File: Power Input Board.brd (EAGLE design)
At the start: 136.7 x 135.2 mm, 10 parts, among them Q1 SPB80P06P

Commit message: put in outline
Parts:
- moved Q1 114.9 mm to (92.7, 36.8)
- moved D4 112.0 mm to (80.0, 27.9)
- moved U$1 107.3 mm to (72.4, 38.1)
- moved R3 92.7 mm to (69.8, 26.7)
- moved D2 83.3 mm to (62.2, 33.0)
- moved D3 82.9 mm to (55.9, 38.1)
- moved D1 79.5 mm to (62.2, 39.4)
- moved R2 76.3 mm to (57.1, 31.8)
- moved R1 76.2 mm to (61.0, 27.9)
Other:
- board size 136.7 x 135.2 mm -> 136.7 x 125.3 mm

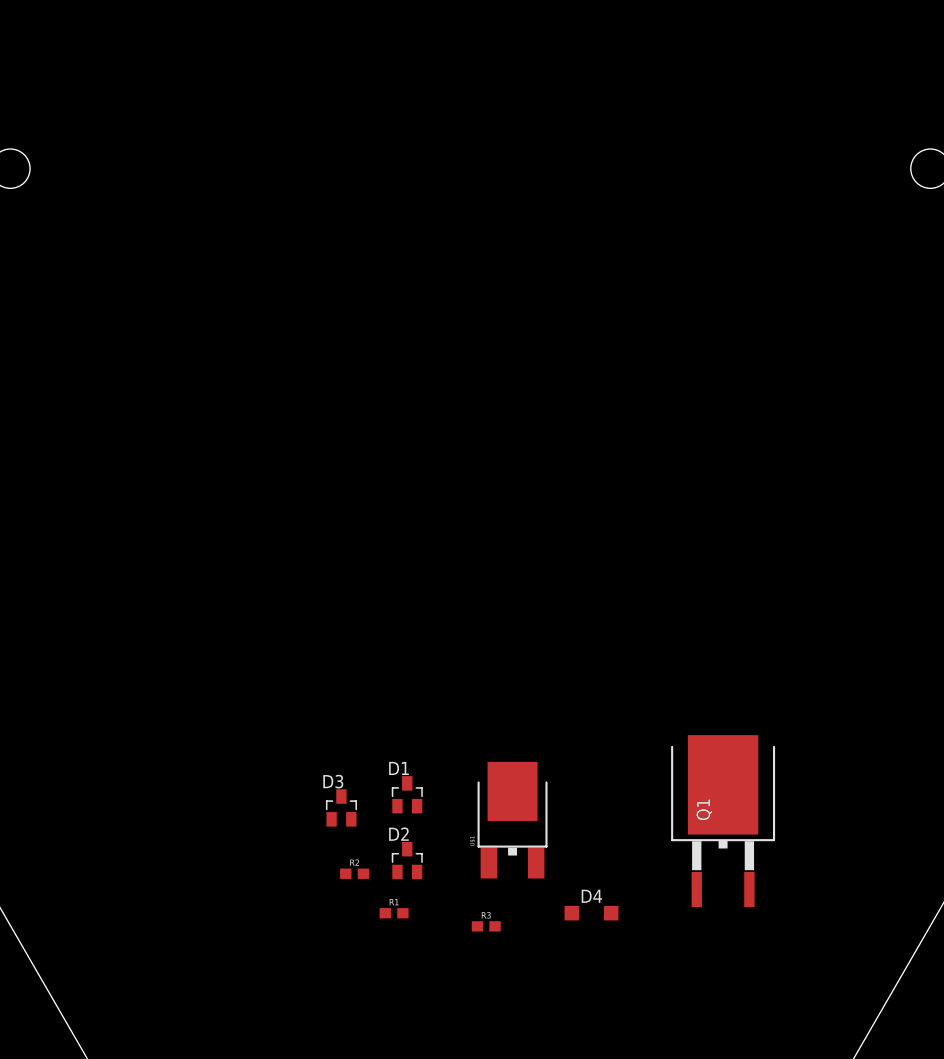
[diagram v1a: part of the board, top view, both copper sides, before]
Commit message: added brick outlines
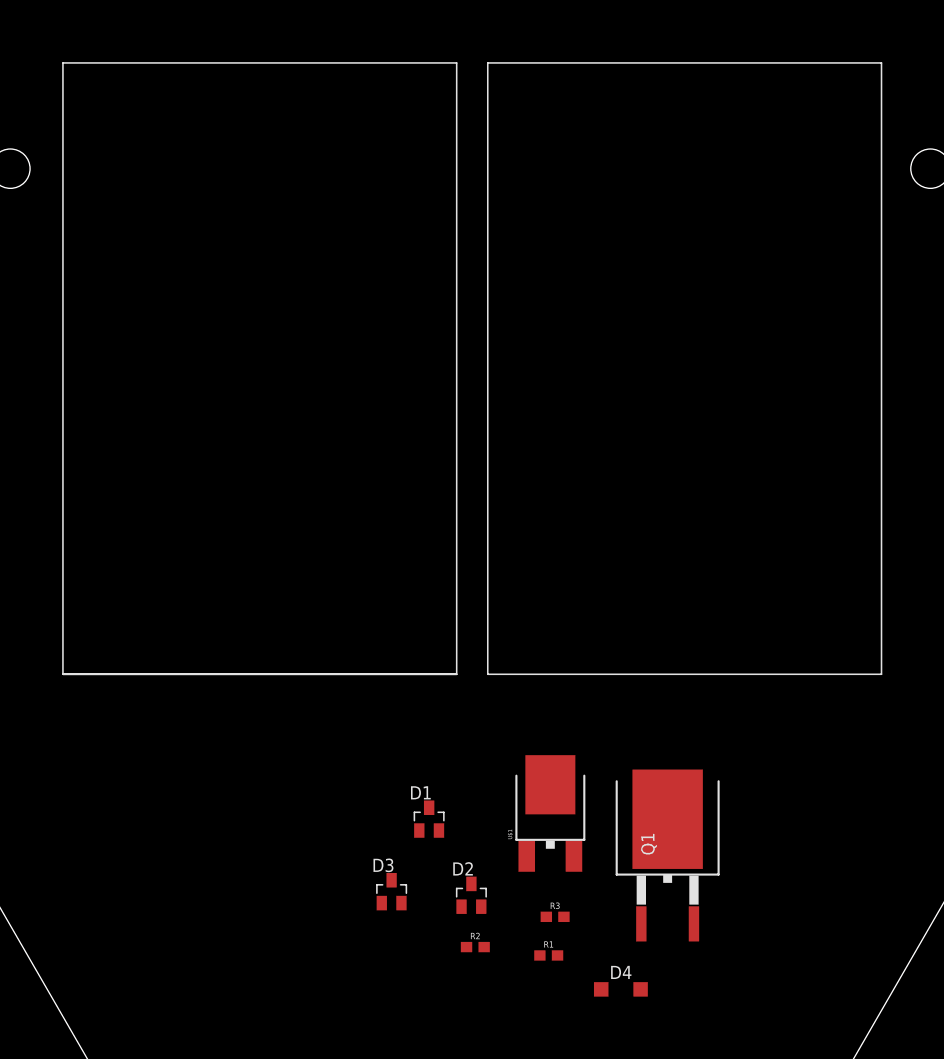
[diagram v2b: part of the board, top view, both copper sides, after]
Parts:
- moved R1 15.5 mm to (75.9, 23.9)
- moved R2 13.6 mm to (68.8, 24.7)
- moved D3 9.42 mm to (60.7, 30.0)
- moved D4 7.88 mm to (82.8, 20.6)
- moved D2 7.04 mm to (68.4, 29.7)
- moved R3 6.71 mm to (76.5, 27.6)
- moved Q1 6.30 mm to (87.4, 33.5)
- moved U$1 3.71 mm to (76.0, 38.8)
- moved D1 3.16 mm to (64.3, 37.0)

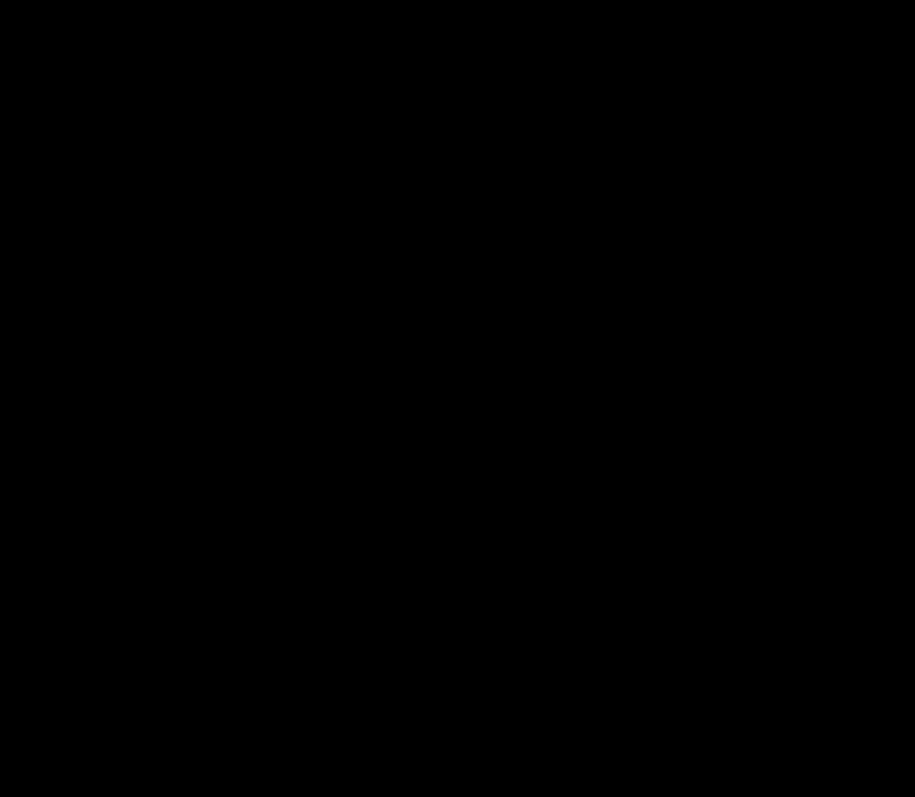
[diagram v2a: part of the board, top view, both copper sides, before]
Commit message: inserted diodes
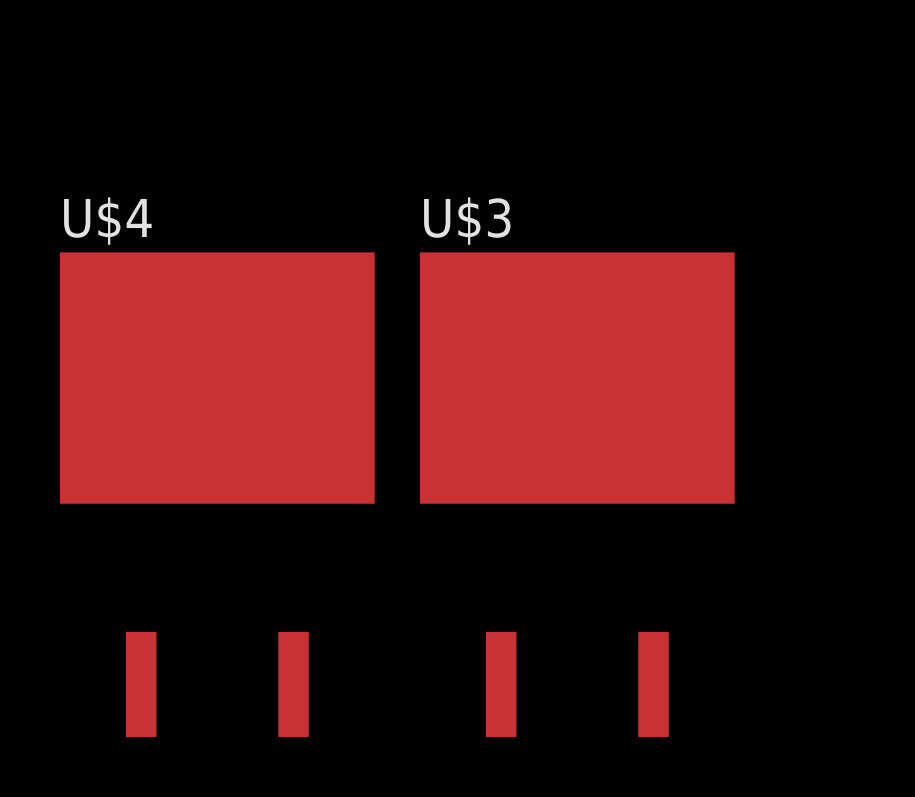
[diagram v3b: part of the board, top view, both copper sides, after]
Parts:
- added U$3, U$4: DIODE, DIODE:DIODE
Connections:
- new net +12V: U$3.OUT, U$4.OUT
- new net +12V_1: U$3.IN1, U$3.IN2
- new net +12V_2: U$4.IN1, U$4.IN2
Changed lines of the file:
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@@
 </element>
 <element name="U$2" library="board_outlines" package="PDB" value="BOARDPDB" x="0" y="0"/>
+<element name="U$3" library="DIODE" package="DIODE" value="DIODE" x="-12" y="7"/>
+<element name="U$4" library="DIODE" package="DIODE" value="DIODE" x="-24" y="7"/>
 </elements>
 <signals>
@@
 <contactref element="Q1" pad="1"/>
 </signal>
+<signal name="+12V_1">
+<contactref element="U$3" pad="IN1"/>
+<contactref element="U$3" pad="IN2"/>
+<wire x1="-4.215" y1="0.977" x2="-9.295" y2="0.977" width="0" layer="19" extent="1-1"/>
+</signal>
+<signal name="+12V_2">
+<contactref element="U$4" pad="IN1"/>
+<contactref element="U$4" pad="IN2"/>
+<wire x1="-16.215" y1="0.977" x2="-21.295" y2="0.977" width="0" layer="19" extent="1-1"/>
+</signal>
+<signal name="+12V">
+<contactref element="U$3" pad="OUT"/>
+<contactref element="U$4" pad="OUT"/>
+<wire x1="-6.755" y1="11.19" x2="-18.755" y2="11.19" width="0" layer="19" extent="1-1"/>
+</signal>
 </signals>

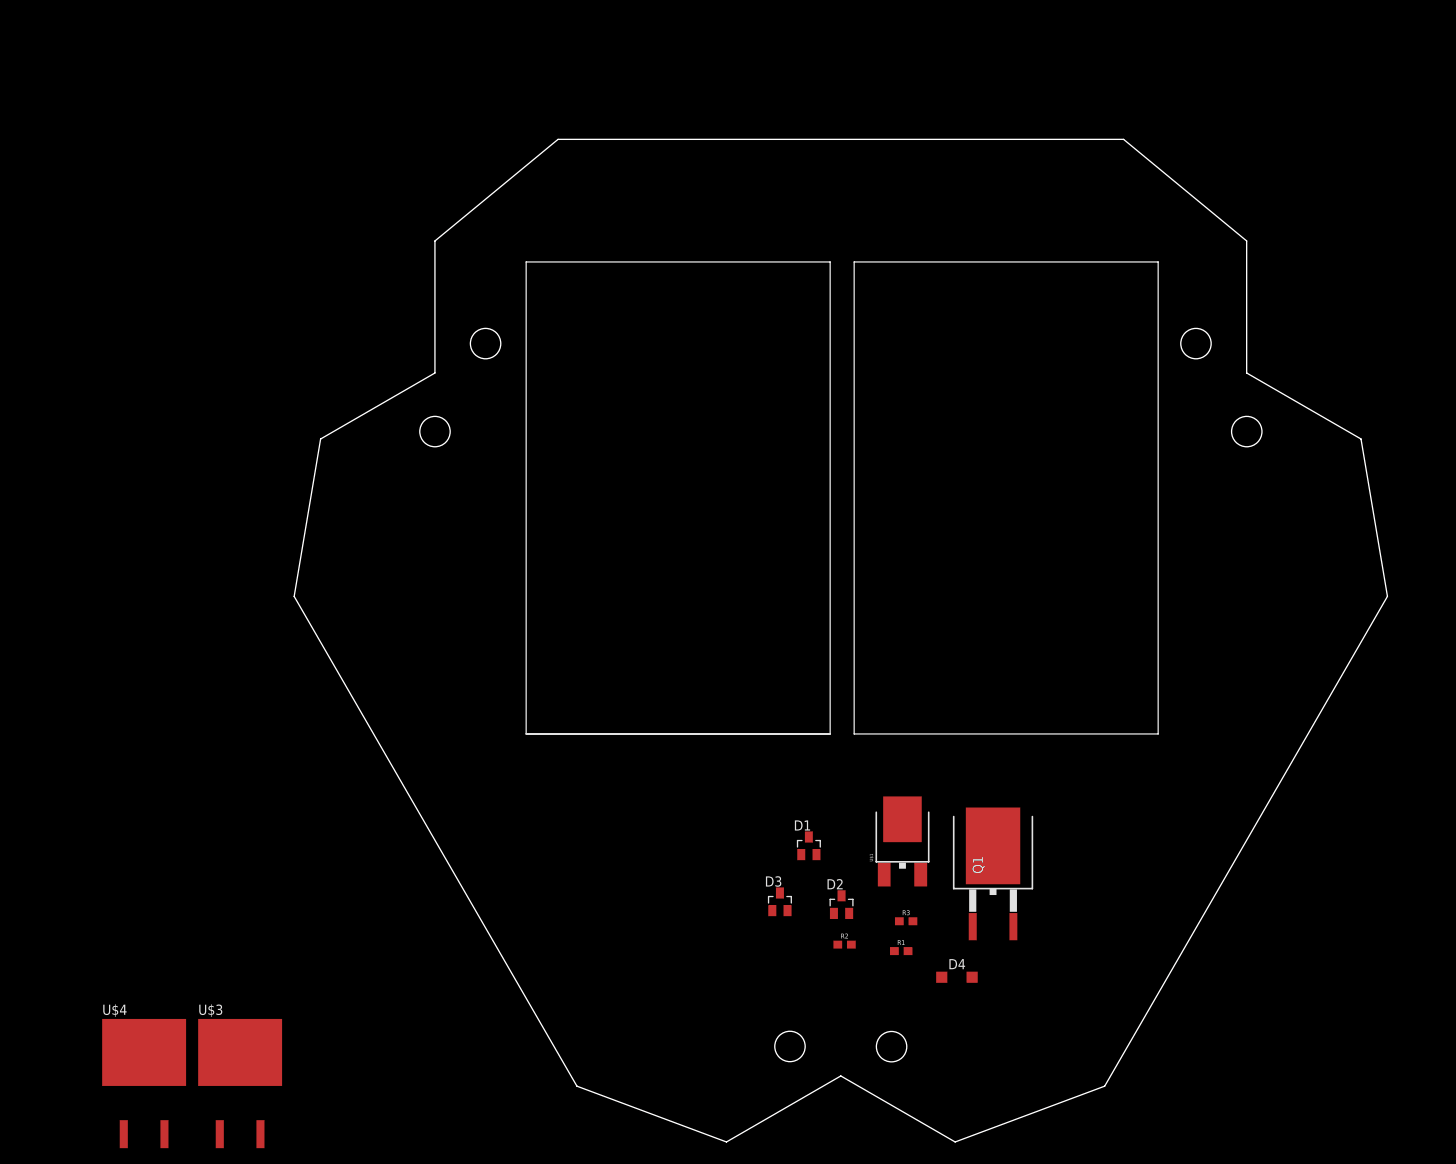
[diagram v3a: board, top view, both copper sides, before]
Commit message: put the connectors on the board
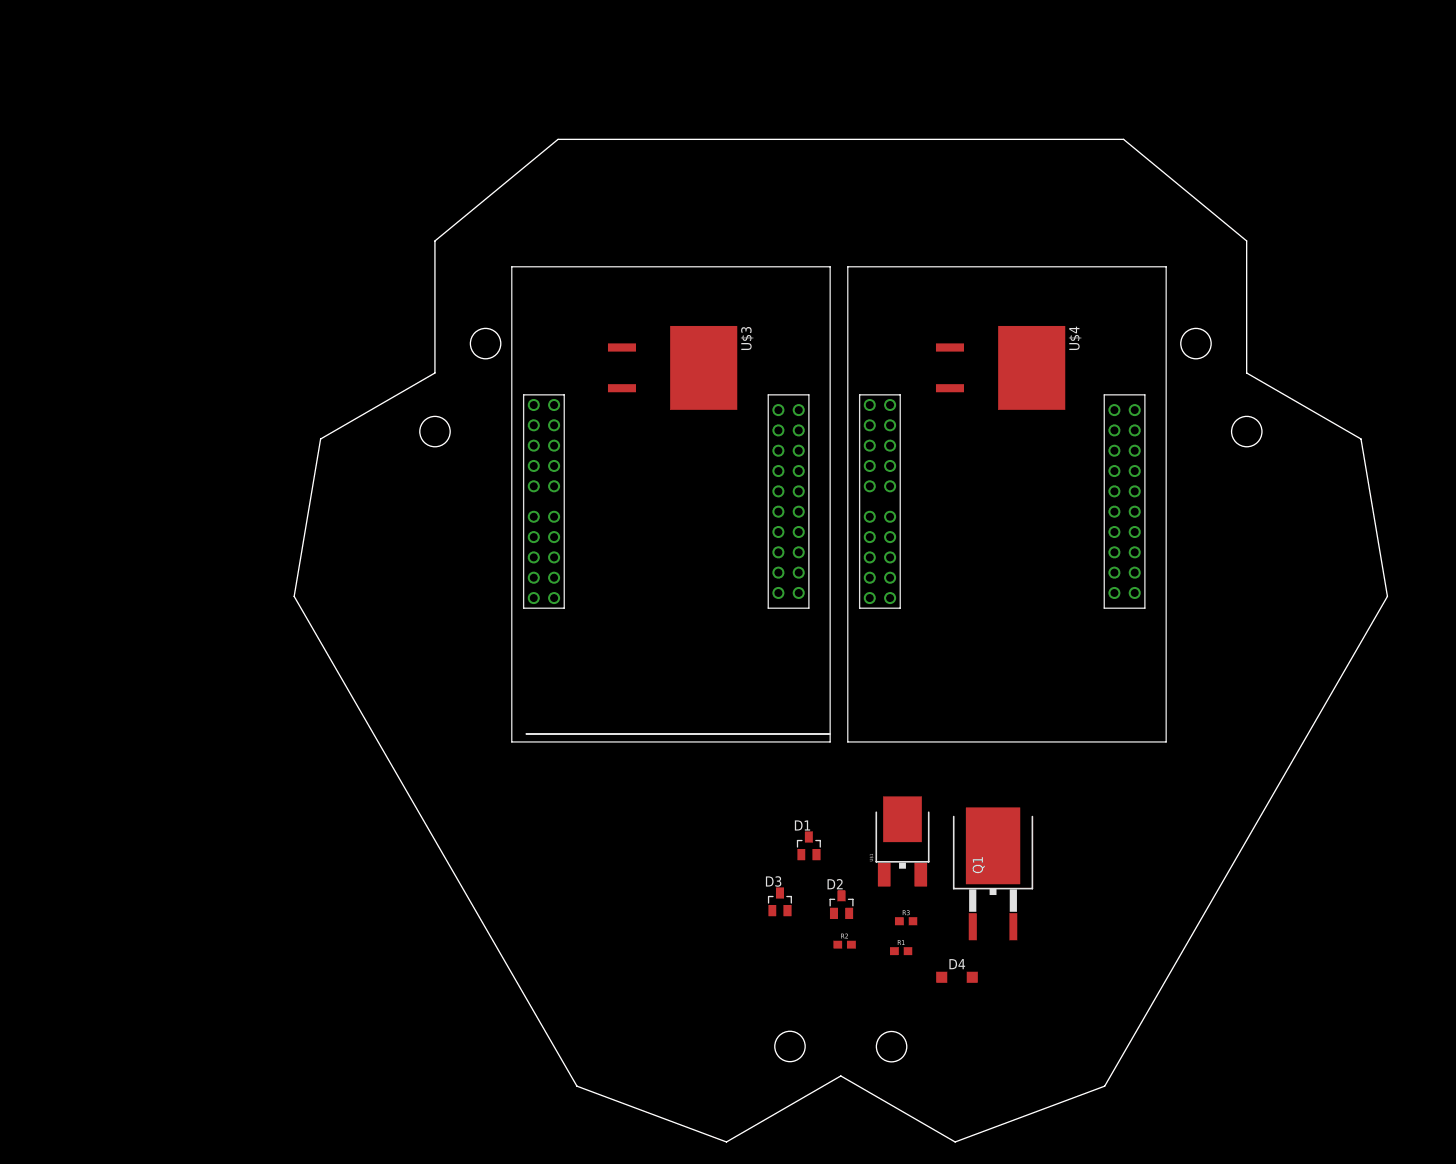
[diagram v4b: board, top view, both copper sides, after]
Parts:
- added U$5, U$6: BRICK_TO_POWER_DIST_WHOLE, PDB_TO_BRICKS:BRICK_TO_POWER_DIST_WHOLE
- moved U$4 146.9 mm to (88.0, 102.0), turned to 270 degrees
- moved U$3 111.8 mm to (47.0, 102.0), turned to 270 degrees
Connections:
- new net GND: U$5.GND1, U$5.GND10, U$5.GND2, U$5.GND3, U$5.GND4, U$5.GND5, U$5.GND6, U$5.GND7, U$5.GND8, U$5.GND9, U$6.GND1, U$6.GND10, U$6.GND2, U$6.GND3, U$6.GND4, U$6.GND5, U$6.GND6, U$6.GND7, U$6.GND8, U$6.GND9
- new net N$10: U$5.D_GND
- new net N$12: U$6.48V_GND1, U$6.48V_GND2, U$6.48V_GND3, U$6.48V_GND4
- new net N$13: U$6.D_GND
- new net N$9: U$5.48V_GND1, U$5.48V_GND2, U$5.48V_GND3, U$5.48V_GND4
- net +12V_1: now also U$5.+12V1, U$5.+12V10, U$5.+12V2, U$5.+12V3, U$5.+12V4, U$5.+12V5, U$5.+12V6, U$5.+12V7, U$5.+12V8, U$5.+12V9
- net +12V_2: now also U$6.+12V1, U$6.+12V10, U$6.+12V2, U$6.+12V3, U$6.+12V4, U$6.+12V5, U$6.+12V6, U$6.+12V7, U$6.+12V8, U$6.+12V9
- net +48V: now also U$5.+48V1, U$5.+48V2, U$5.+48V3, U$5.+48V4, U$6.+48V1, U$6.+48V2, U$6.+48V3, U$6.+48V4
- net ON/OFF: now also U$5.ON/OFF, U$6.ON/OFF

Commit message: reconstructing
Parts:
- added J1, J2: (no value), SparkFun-Connectors:BANANA_CONN
- moved U$5 70.7 mm to (28.0, 109.0), turned to 270 degrees
- moved U$6 70.7 mm to (70.0, 109.0), turned to 270 degrees
- moved R1 25.2 mm to (52.1, 32.1), turned to 180 degrees
- moved U$1 24.2 mm to (52.0, 41.8)
- moved D4 22.6 mm to (74.2, 41.4), turned to 180 degrees
- moved D1 17.7 mm to (50.0, 26.7), turned to 270 degrees
- moved D2 10.4 mm to (58.4, 32.7)
- moved R3 8.18 mm to (74.4, 35.5), turned to 90 degrees
- moved R2 7.54 mm to (63.7, 30.2), turned to 270 degrees
- moved D3 5.26 mm to (57.0, 26.3), turned to 270 degrees
- moved Q1 5.26 mm to (88.5, 38.6), turned to 270 degrees
- moved U$3 5.00 mm to (43.0, 99.0), turned to 0 degrees
- moved U$4 3.61 mm to (86.0, 99.0), turned to 0 degrees
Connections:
- net N$12 renamed +48V_GND
- removed net N$9: U$5.48V_GND1, U$5.48V_GND2, U$5.48V_GND3, U$5.48V_GND4
- removed net VCC: Q1.1
- new net +48V_RAW: J1.P$1, Q1.1
- new net 48V_GND: J2.P$1, R3.1, U$5.48V_GND1, U$5.48V_GND2, U$5.48V_GND3, U$5.48V_GND4
- net 3.3V: no longer R3.1
